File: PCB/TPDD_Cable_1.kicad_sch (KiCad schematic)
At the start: 0 parts

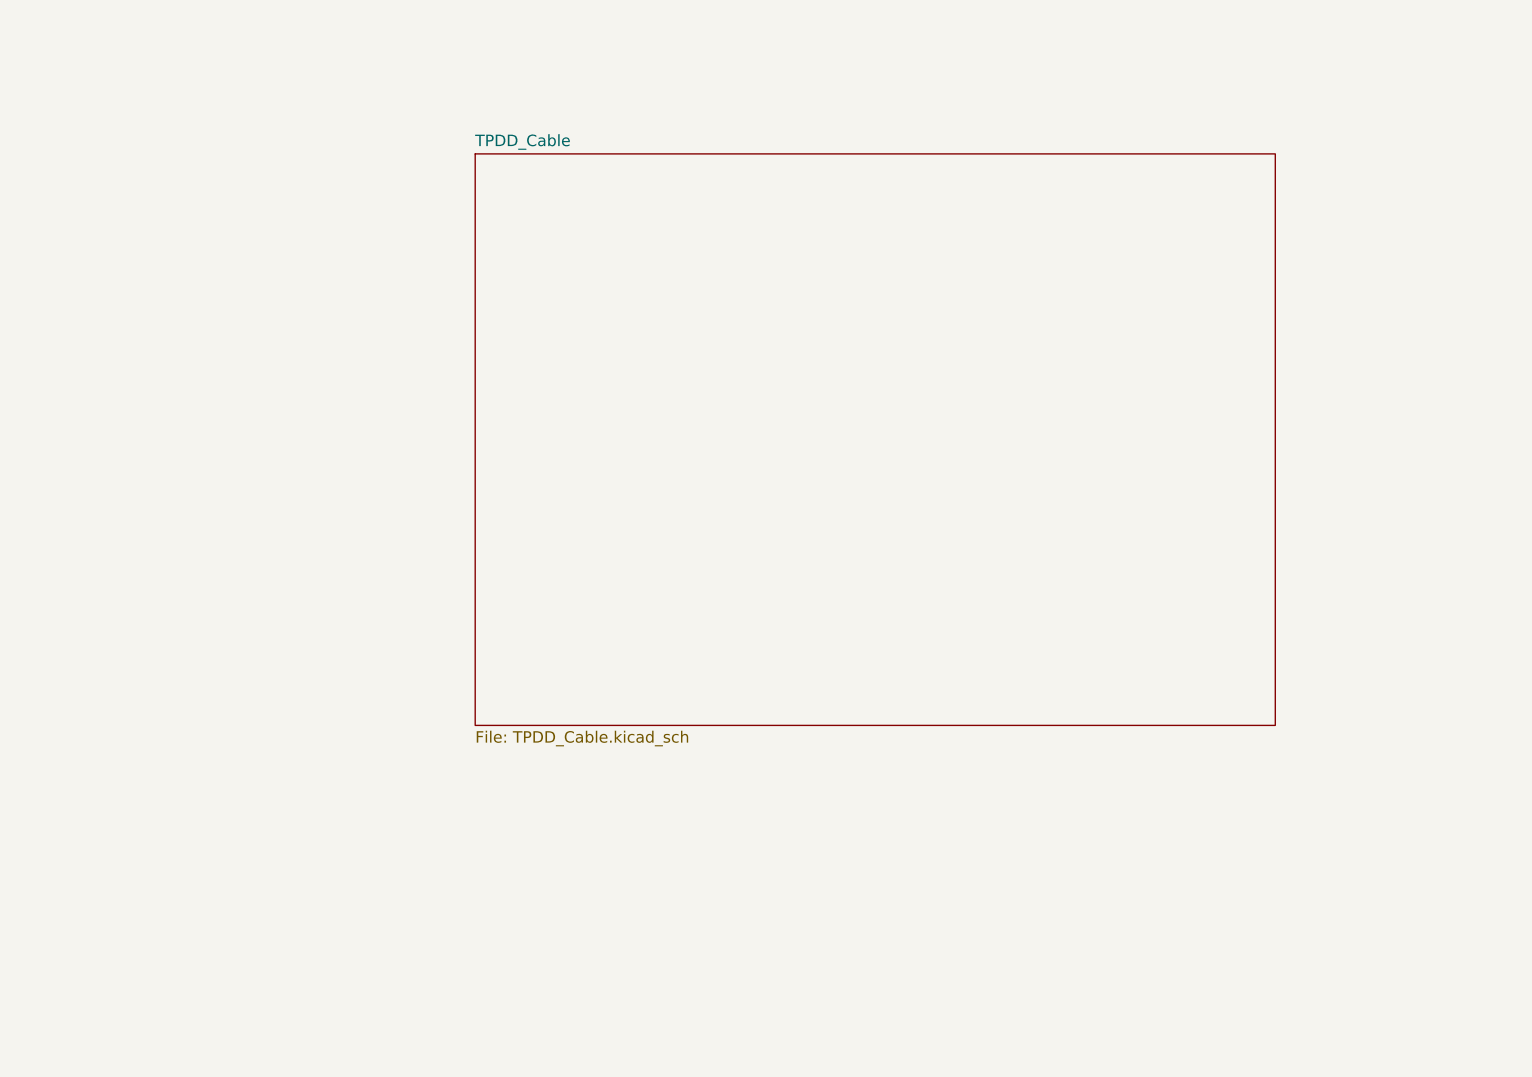
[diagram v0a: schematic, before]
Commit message: pcb 2 is new default, smt wire pads
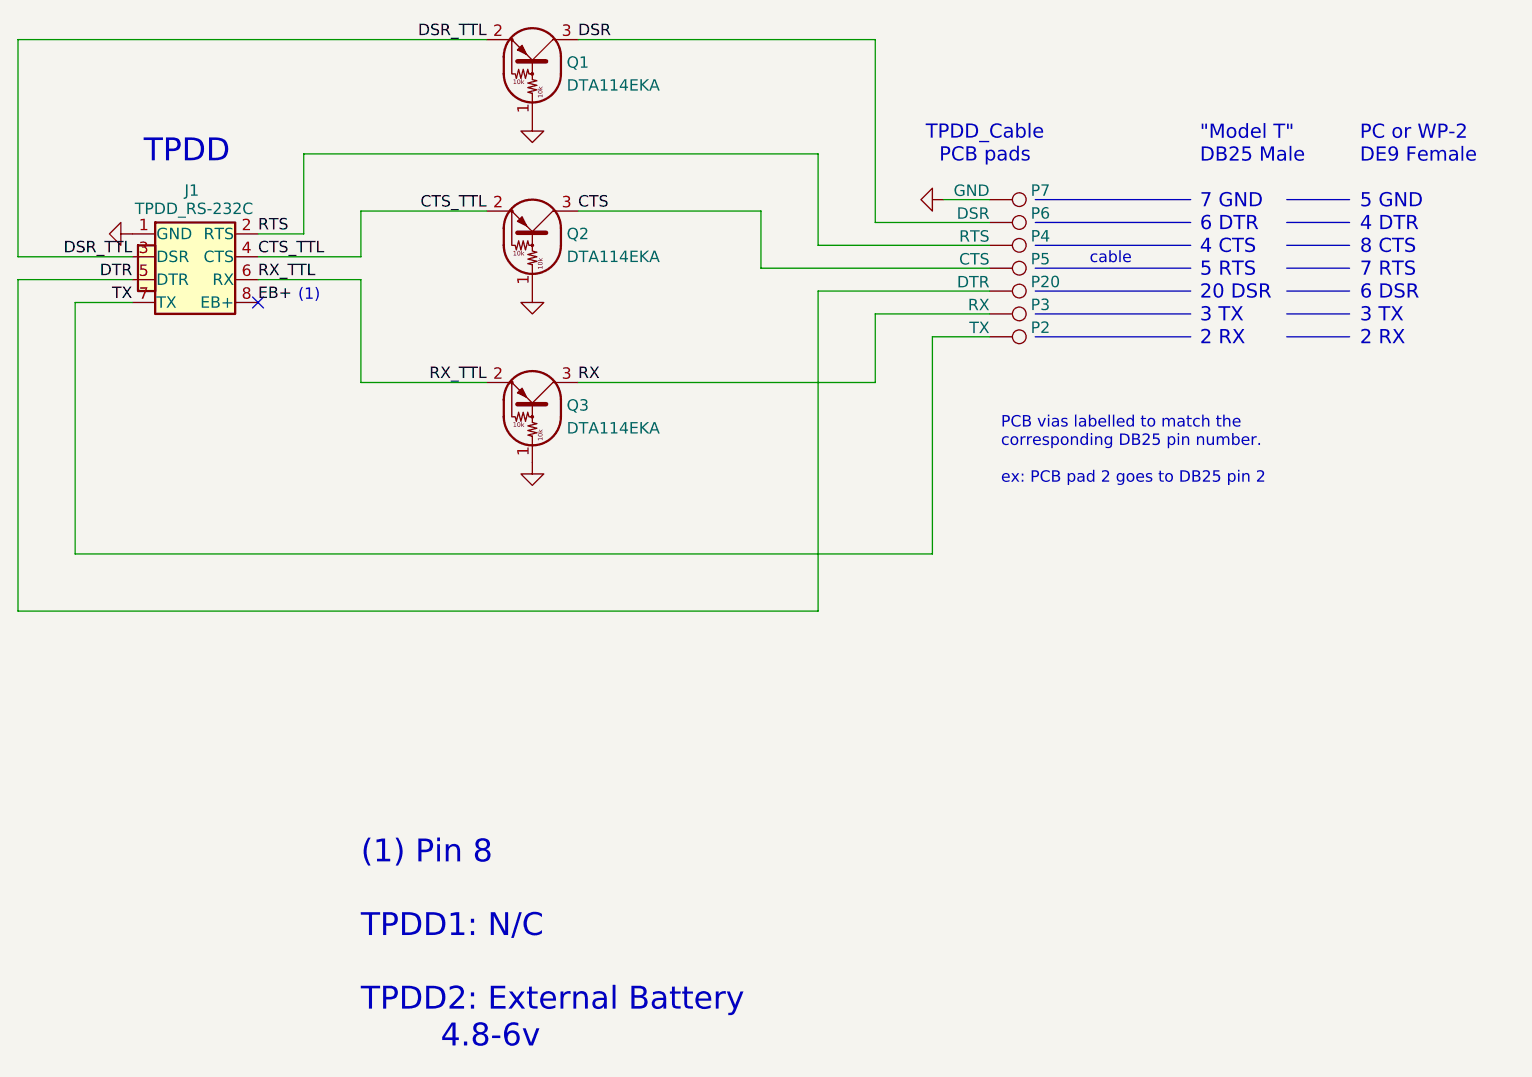
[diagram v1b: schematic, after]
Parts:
- added J1: TPDD_RS-232C, 000_LOCAL:2x4x2.54mm_edge_mount, symbol 000_LOCAL:TPDD_RS-232C
- added P2: TX, 000_LOCAL:SMD_1.2x3, symbol 000_LOCAL:TestPoint
- added P20: DTR, 000_LOCAL:PTH_0.65x1.2, symbol 000_LOCAL:TestPoint
- added P3: RX, 000_LOCAL:SMD_1.2x3, symbol 000_LOCAL:TestPoint
- added P4: RTS, 000_LOCAL:PTH_0.65x1.2, symbol 000_LOCAL:TestPoint
- added P5: CTS, 000_LOCAL:PTH_0.65x1.2, symbol 000_LOCAL:TestPoint
- added P6: DSR, 000_LOCAL:PTH_0.65x1.2, symbol 000_LOCAL:TestPoint
- added P7: GND, 000_LOCAL:PTH_0.65x1.2, symbol 000_LOCAL:TestPoint
- added Q1, Q2, Q3: DTA114EKA, 000_LOCAL:SC-59, symbol 000_LOCAL:Transistor_BJT_DTA114E
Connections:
- new net CTS: P5.1, Q2.3 (C)
- new net CTS_TTL: J1.4 (CTS), Q2.2 (E)
- new net DSR: P6.1, Q1.3 (C)
- new net DSR_TTL: J1.3 (DSR), Q1.2 (E)
- new net DTR: J1.5 (DTR), P20.1
- new net EB+: J1.8 (EB+)
- new net GND: J1.1 (GND), P7.1, Q1.1 (B), Q2.1 (B), Q3.1 (B)
- new net RTS: J1.2 (RTS), P4.1
- new net RX: P3.1, Q3.3 (C)
- new net RX_TTL: J1.6 (RX), Q3.2 (E)
- new net TX: J1.7 (TX), P2.1
- no-connect marks 0 -> 1
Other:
- removed sheet TPDD_Cable
- note added: ""Model T" DB25 Male 7 GND 6 DTR 4 CTS 5 RTS 20 DSR 3 TX 2 RX"
- note added: "(1)"
- note added: "(1) Pin 8 TPDD1: N/C TPDD2: External Battery 4.8-6v"
- note added: "PC or WP-2 DE9 Female 5 GND 4 DTR 8 CTS 7 RTS 6 DSR 3 TX 2 RX"
- note added: "PCB vias labelled to match the corresponding DB25 pin number. ex: PCB pad 2 goes to DB25 pin 2"
- note added: "TPDD"
- note added: "TPDD_Cable PCB pads"
- note added: "cable"

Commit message: schematics notes text
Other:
- note added: ""Model T" DB25 Male 7 6 4 5 20 3 2"
- note added: "PC or WP-2 DE9 Female 5 6 7 8 4 2 3"
- note removed: ""Model T" DB25 Male 7 GND 6 DTR 4 CTS 5 RTS 20 DSR 3 TX 2 RX"
- note removed: "PC or WP-2 DE9 Female 5 GND 4 DTR 8 CTS 7 RTS 6 DSR 3 TX 2 RX"
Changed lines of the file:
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@@
 		)
 	)
-	(text "\"Model T\"\nDB25 Male\n\n7 GND\n6 DTR\n4 CTS\n5 RTS\n20 DSR\n3 TX\n2 RX"
+	(text "\"Model T\"\nDB25 Male\n\n7\n6\n4\n5\n20\n3\n2"
 		(exclude_from_sim no)
 		(at 194.818 72.644 0)
@@
 		)
 	)
-	(text "PC or WP-2\nDE9 Female\n\n5 GND\n4 DTR\n8 CTS\n7 RTS\n6 DSR\n3 TX\n2 RX"
+	(text "PC or WP-2\nDE9 Female\n\n5\n6\n7\n8\n4\n2\n3"
 		(exclude_from_sim no)
 		(at 212.598 72.644 0)
